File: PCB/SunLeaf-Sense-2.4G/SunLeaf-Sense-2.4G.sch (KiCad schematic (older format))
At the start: 0 parts

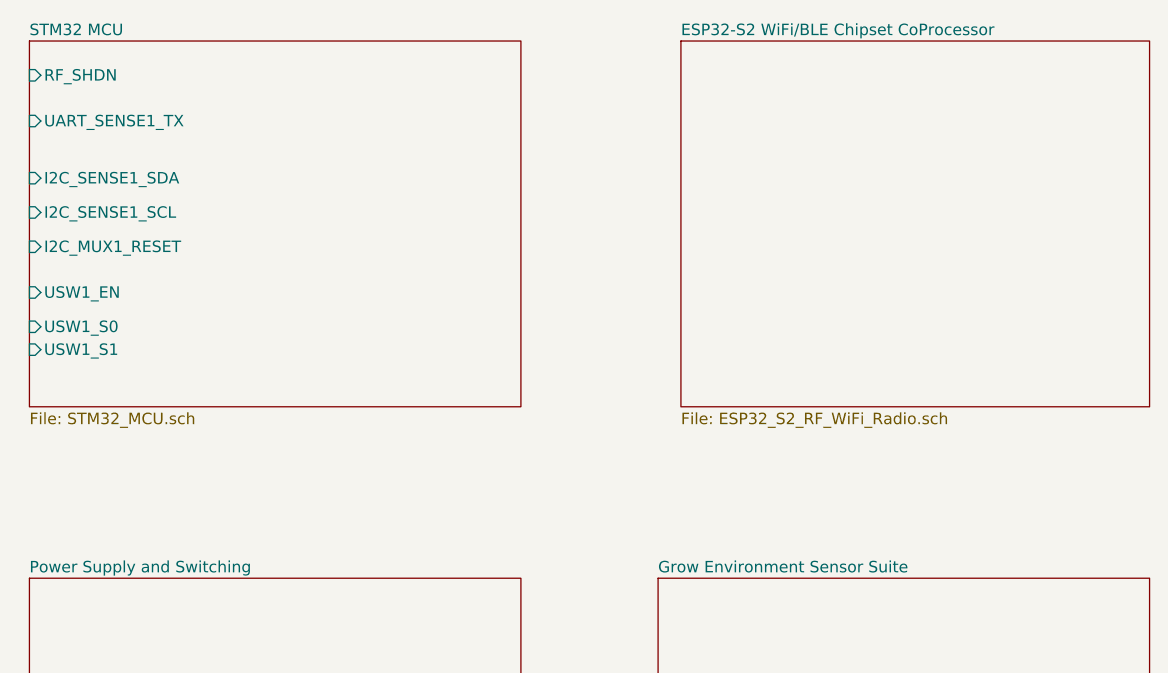
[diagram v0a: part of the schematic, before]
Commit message: Sensors Added
Sensors added to schematic page, project setup around new 2G module from ST
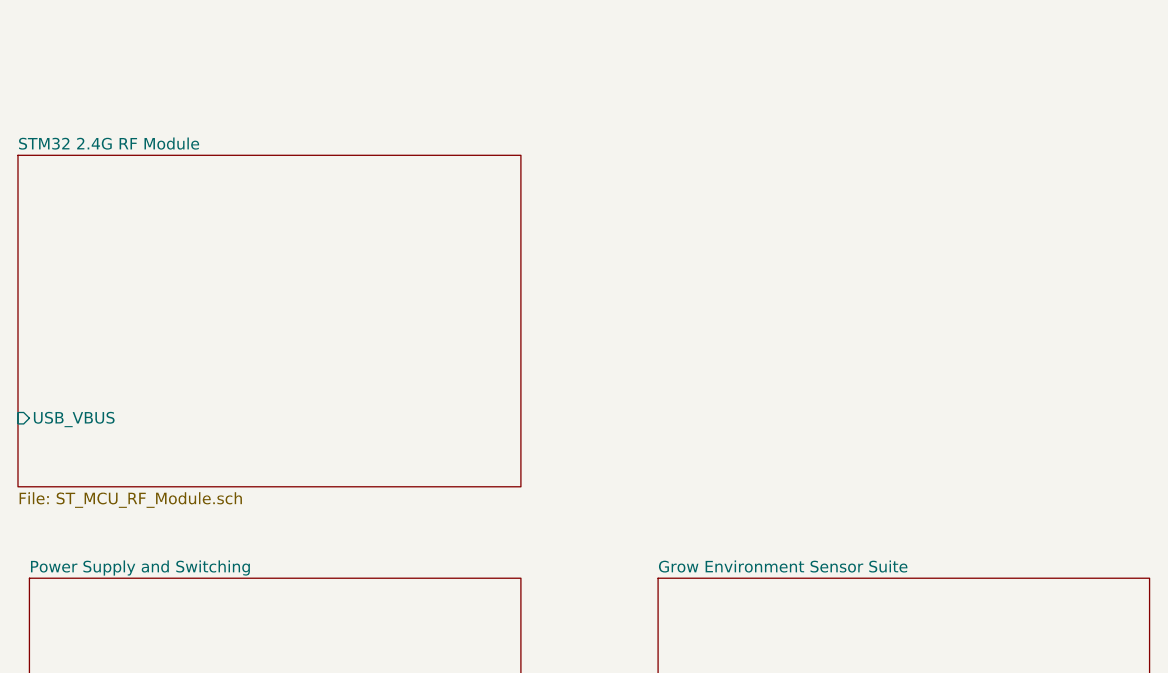
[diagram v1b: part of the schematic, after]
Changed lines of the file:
@@
 $Descr A4 11693 8268
 encoding utf-8
-Sheet 1 5
+Sheet 1 4
 Title ""
 Date ""
@@
 Comment4 ""
 $EndDescr
-$Sheet
-S 2900 2000 2150 1600
-U 6028AFD2
-F0 "STM32 MCU" 50
-F1 "STM32_MCU.sch" 50
-F2 "UART_SENSE1_TX" I L 2900 2350 50
-F3 "I2C_SENSE1_SDA" I L 2900 2600 50
-F4 "I2C_SENSE1_SCL" I L 2900 2750 50
-F5 "I2C_MUX1_RESET" I L 2900 2900 50
-F6 "USW1_EN" I L 2900 3100 50
-F7 "USW1_S0" I L 2900 3250 50
-F8 "USW1_S1" I L 2900 3350 50
-F9 "RF_SHDN" I L 2900 2150 50
-$EndSheet
-$Sheet
-S 5750 2000 2050 1600
-U 6028B0AC
-F0 "ESP32-S2 WiFi/BLE Chipset CoProcessor" 50
-F1 "ESP32_S2_RF_WiFi_Radio.sch" 50
-$EndSheet
 $Sheet
 S 2900 4350 2150 1350
@@
 F1 "Sensor_Suite.sch" 50
 $EndSheet
+$Sheet
+S 2850 2500 2200 1450
+U 60383D67
+F0 "STM32 2.4G RF Module" 50
+F1 "ST_MCU_RF_Module.sch" 50
+F2 "USB_VBUS" I L 2850 3650 50
+$EndSheet
 $EndSCHEMATC

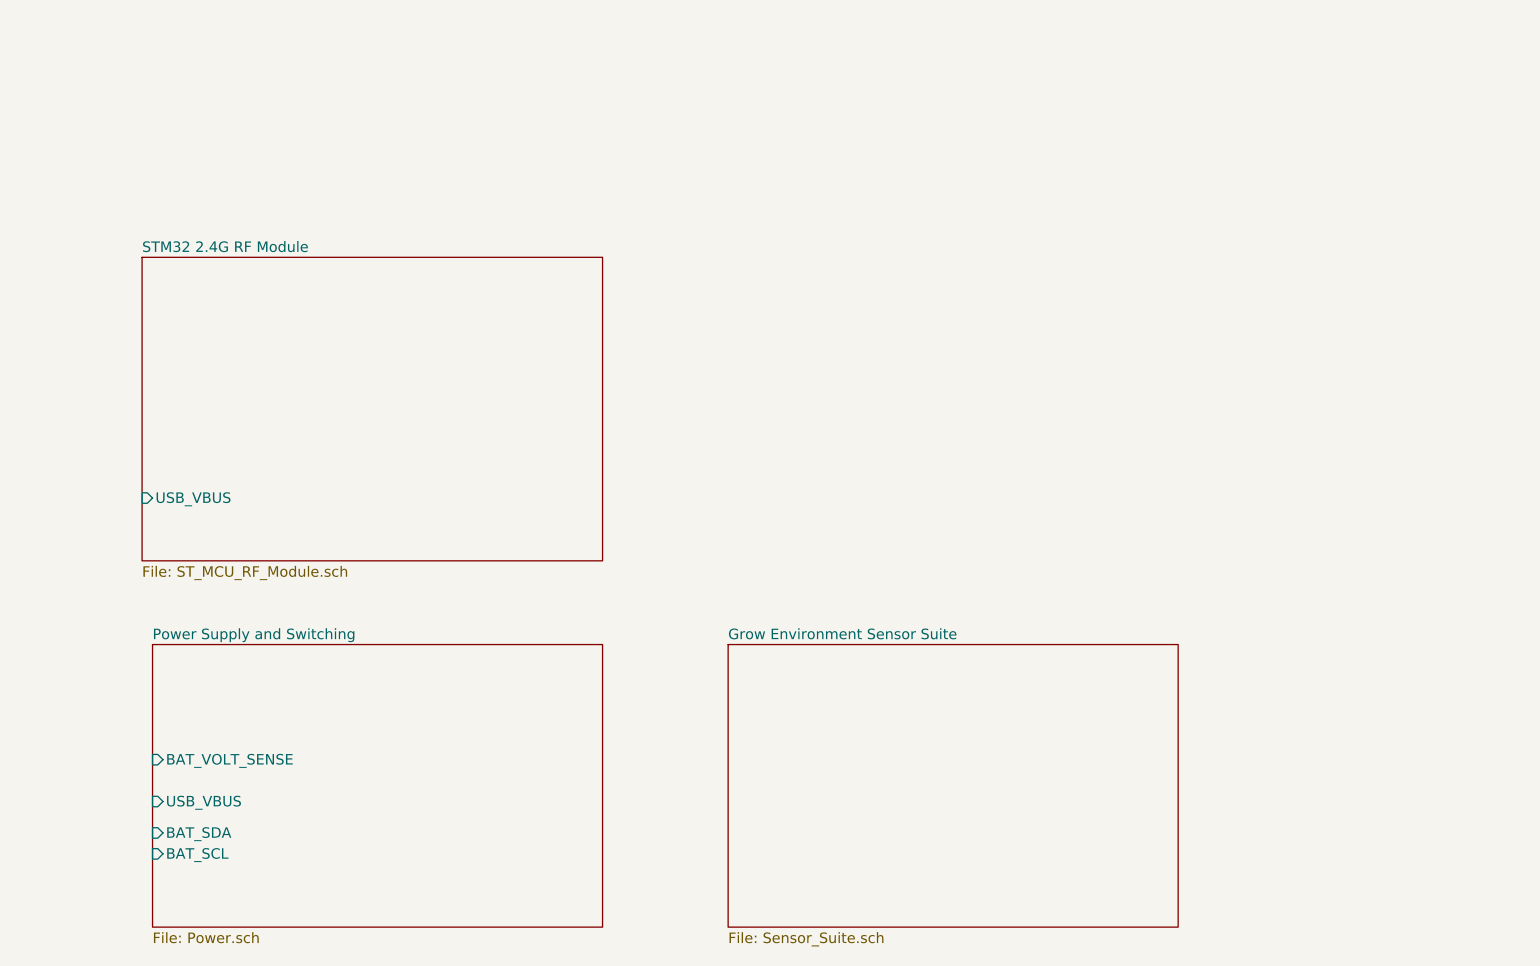
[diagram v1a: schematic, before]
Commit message: PCB
PCB started, PAR sensor circuitry integrated into design
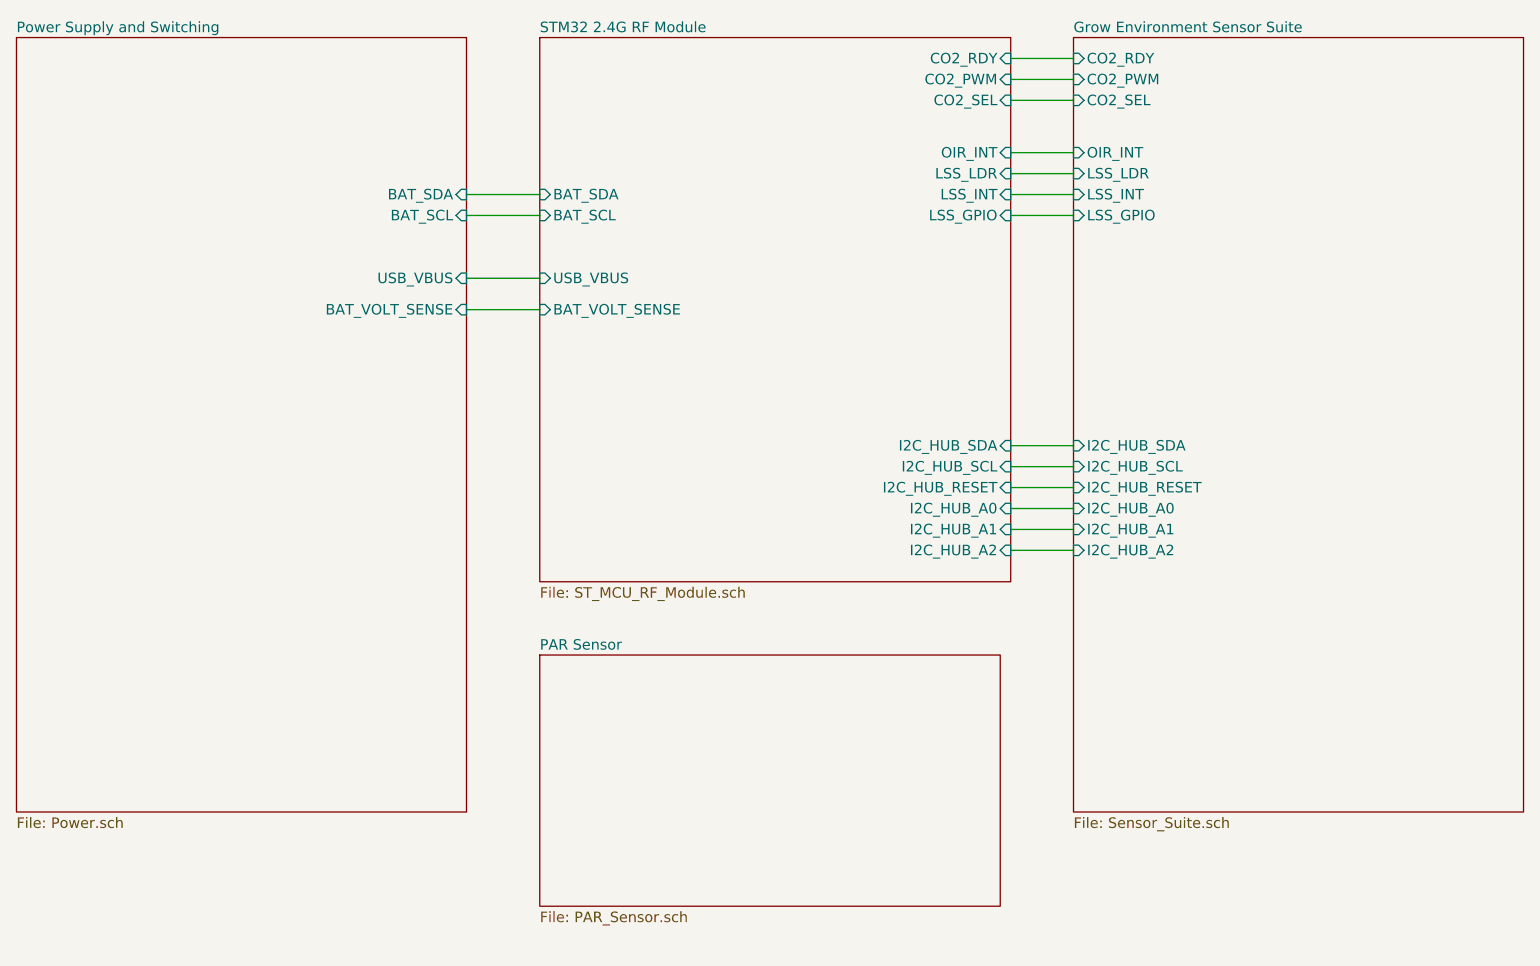
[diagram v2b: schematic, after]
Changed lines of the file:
@@
 $Descr A4 11693 8268
 encoding utf-8
-Sheet 1 4
+Sheet 1 5
 Title ""
 Date ""
@@
 $EndDescr
 $Sheet
-S 2900 4350 2150 1350
+S 2250 1450 2150 3700
 U 6028B309
 F0 "Power Supply and Switching" 50
 F1 "Power.sch" 50
-F2 "BAT_VOLT_SENSE" I L 2900 4900 50
-F3 "USB_VBUS" I L 2900 5100 50
-F4 "BAT_SDA" I L 2900 5250 50
-F5 "BAT_SCL" I L 2900 5350 50
+F2 "BAT_VOLT_SENSE" I R 4400 2750 50
+F3 "USB_VBUS" I R 4400 2600 50
+F4 "BAT_SDA" I R 4400 2200 50
+F5 "BAT_SCL" I R 4400 2300 50
 $EndSheet
+Wire Wire Line
+	4400 2750 4750 2750
+Wire Wire Line
+	4400 2200 4750 2200
+Wire Wire Line
+	4750 2300 4400 2300
+Wire Wire Line
+	4400 2600 4750 2600
 $Sheet
-S 5650 4350 2150 1350
+S 7300 1450 2150 3700
 U 6028B457
 F0 "Grow Environment Sensor Suite" 50
 F1 "Sensor_Suite.sch" 50
+F2 "CO2_RDY" I L 7300 1550 50
+F3 "CO2_PWM" I L 7300 1650 50
+F4 "CO2_SEL" I L 7300 1750 50
+F5 "OIR_INT" I L 7300 2000 50
+F6 "LSS_LDR" I L 7300 2100 50
+F7 "LSS_INT" I L 7300 2200 50
+F8 "I2C_HUB_SDA" I L 7300 3400 50
+F9 "I2C_HUB_SCL" I L 7300 3500 50
+F10 "I2C_HUB_RESET" I L 7300 3600 50
+F11 "I2C_HUB_A0" I L 7300 3700 50
+F12 "I2C_HUB_A1" I L 7300 3800 50
+F13 "I2C_HUB_A2" I L 7300 3900 50
+F14 "LSS_GPIO" I L 7300 2300 50
 $EndSheet
 $Sheet
-S 2850 2500 2200 1450
+S 4750 1450 2250 2600
 U 60383D67
 F0 "STM32 2.4G RF Module" 50
 F1 "ST_MCU_RF_Module.sch" 50
-F2 "USB_VBUS" I L 2850 3650 50
+F2 "USB_VBUS" I L 4750 2600 50
+F3 "BAT_VOLT_SENSE" I L 4750 2750 50
+F4 "BAT_SDA" I L 4750 2200 50
+F5 "BAT_SCL" I L 4750 2300 50
+F6 "I2C_HUB_SDA" I R 7000 3400 50
+F7 "I2C_HUB_SCL" I R 7000 3500 50
+F8 "I2C_HUB_RESET" I R 7000 3600 50
+F9 "I2C_HUB_A0" I R 7000 3700 50
+F10 "I2C_HUB_A1" I R 7000 3800 50
+F11 "I2C_HUB_A2" I R 7000 3900 50
+F12 "CO2_RDY" I R 7000 1550 50
+F13 "CO2_PWM" I R 7000 1650 50
+F14 "CO2_SEL" I R 7000 1750 50
+F15 "LSS_LDR" I R 7000 2100 50
+F16 "LSS_INT" I R 7000 2200 50
+F17 "OIR_INT" I R 7000 2000 50
+F18 "LSS_GPIO" I R 7000 2300 50
+$EndSheet
+Wire Wire Line
+	7000 3400 7300 3400
+Wire Wire Line
+	7000 3500 7300 3500
+Wire Wire Line
+	7300 3600 7000 3600
+Wire Wire Line
+	7000 3700 7300 3700
+Wire Wire Line
+	7300 3800 7000 3800
+Wire Wire Line
+	7000 3900 7300 3900
+Wire Wire Line
+	7300 2000 7000 2000
+Wire Wire Line
+	7000 2100 7300 2100
+Wire Wire Line
+	7300 2200 7000 2200
+Wire Wire Line
+	7000 1750 7300 1750
+Wire Wire Line
+	7000 1650 7300 1650
+Wire Wire Line
+	7000 1550 7300 1550
+Wire Wire Line
+	7000 2300 7300 2300
+$Sheet
+S 4750 4400 2200 1200
+U 60568996
+F0 "PAR Sensor" 50
+F1 "PAR_Sensor.sch" 50
 $EndSheet
 $EndSCHEMATC
